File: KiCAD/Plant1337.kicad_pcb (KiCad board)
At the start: 4 copper layers, 59.1 x 41.9 mm, 58 parts, among them J1 USB_B_Micro, J2 Edge2x6_Connector, Q1 AO3400A, Q2 AO3400A, Q3 AO3400A, Q4 AO3400A, U1 SHTC3, U2 ESP32-WROOM-32, U3 AMS1117-3.3

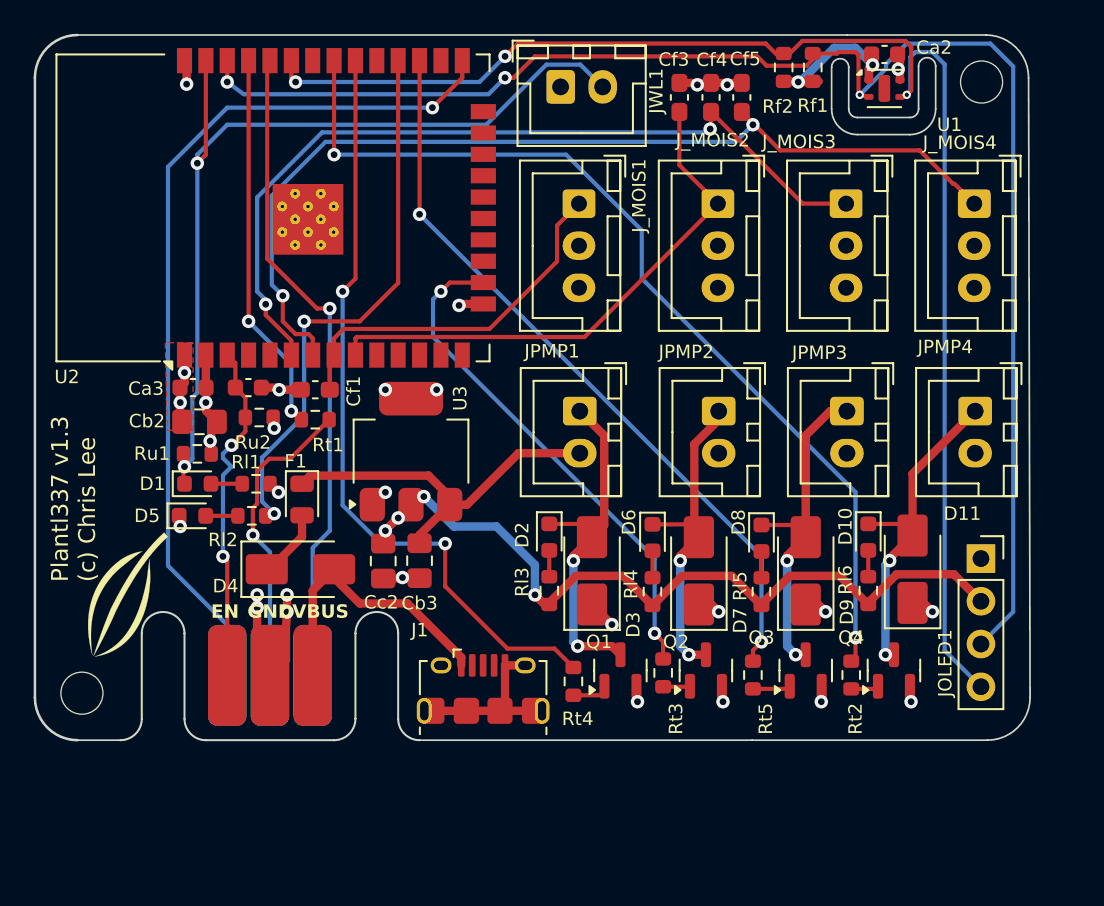
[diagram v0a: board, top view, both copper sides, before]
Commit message: Support for board 2.0: USB-C, ESP32-C3-WROOM1-B8R2
Need to make new board version a new compiler def and ifdef new pin assignments.
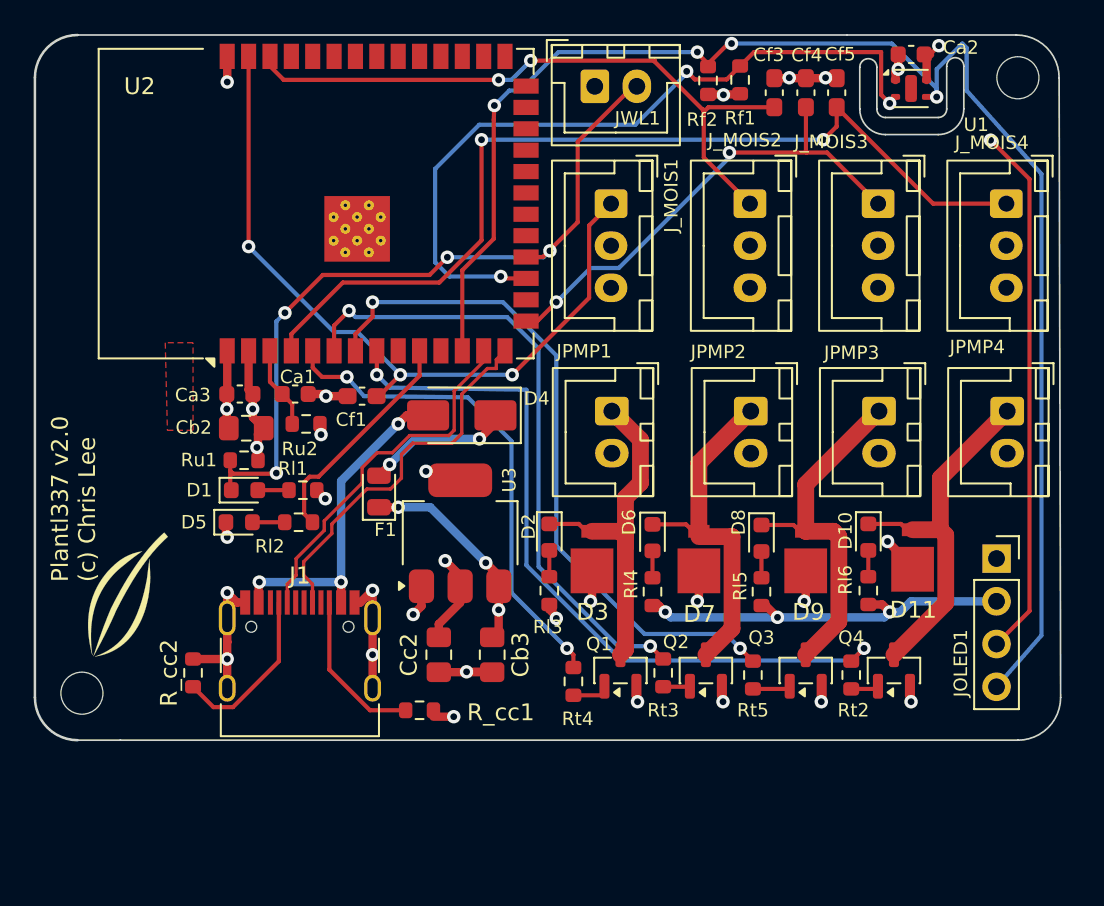
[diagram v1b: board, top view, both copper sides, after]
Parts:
- removed J2: Edge2x6_Connector, Library:EdgeConnector_2x3
- removed Rt1: 470, Resistor_SMD:R_0603_1608Metric
- added R_cc1: 5.1k, Resistor_SMD:R_0603_1608Metric, F.Cu at (69.8, 99.8)
- added R_cc2: 5.1k, Resistor_SMD:R_0603_1608Metric, F.Cu at (56.4, 97.6)
- D11, D3, D7, D9: footprint Diode_SMD:D_SMA -> chl33_library:DO-216
- J1: value USB_B_Micro -> USB_C_Receptacle_USB2.0_16P; footprint Connector_USB:USB_Micro-B_Amphenol_10118194_Horizontal -> Connector_USB:USB_C_Receptacle_HRO_TYPE-C-31-M-12
- U2: value ESP32-WROOM-32 -> ESP32-S3-WROOM-1; footprint RF_Module:ESP32-WROOM-32 -> RF_Module:ESP32-S3-WROOM-1
- moved D4 13.2 mm to (72.4, 82.3), turned to 180 degrees
- moved J1 10.9 mm to (62.7, 97.5)
- moved Cb3 7.06 mm to (74.2, 96.5)
- moved Cc2 6.47 mm to (71.0, 96.5)
- moved U3 5.66 mm to (72.3, 89.3)
- moved Cf3 5.65 mm to (90.9, 63.1)
- moved Cf4 5.65 mm to (92.8, 63.1)
- moved Cf5 5.65 mm to (94.6, 63.1)
- moved F1 4.60 mm to (67.4, 86.8), turned to 90 degrees
- moved Rf2 4.56 mm to (87.0, 62.4)
- moved Rf1 4.38 mm to (88.9, 62.4)
- moved D1 2.81 mm to (59.4, 86.7)
- moved Ca1 2.81 mm to (62.5, 81.0)
- moved Ca3 2.81 mm to (59.2, 81.0)
- moved Cb2 2.81 mm to (59.5, 83.1)
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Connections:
- U2 pad 10: unconnected-(U2-IO25-Pad10) -> GPIO17
- U2 pad 12: unconnected-(U2-IO27-Pad12) -> SDA1
- U2 pad 13: unconnected-(U2-IO14-Pad13) -> USB_D-
- U2 pad 14: unconnected-(U2-IO12-Pad14) -> USB_D+
- U2 pad 15: GND -> ADC1_CH6
- U2 pad 16: P2 -> unconnected-(U2-IO46-Pad16)
- U2 pad 17: unconnected-(U2-SHD/SD2-Pad17) -> SCL1
- U2 pad 18: unconnected-(U2-SWP/SD3-Pad18) -> WL
- U2 pad 25: GPIO0 -> unconnected-(U2-IO48-Pad25)
- U2 pad 27: P3 -> unconnected-(U2-IO0-Pad27)
- U2 pad 28: GPIO17 -> unconnected-(U2-IO35-Pad28)
- U2 pad 30: P1 -> unconnected-(U2-IO37-Pad30)
- U2 pad 31: P4 -> unconnected-(U2-IO38-Pad31)
- U2 pad 33: SDA1 -> unconnected-(U2-IO40-Pad33)
- U2 pad 34: TXC -> unconnected-(U2-IO41-Pad34)
- U2 pad 35: TX -> unconnected-(U2-IO42-Pad35)
- U2 pad 36: SCL1 -> unconnected-(U2-RXD0-Pad36)
- U2 pad 37: WL -> unconnected-(U2-TXD0-Pad37)
- U2 pad 38: GND -> ADC1_CH5
- U2 pad 39: GND -> ADC1_CH4
- U2 pad 4: unconnected-(U2-SENSOR_VP-Pad4) -> ADC1_CH7
- U2 pad 5: unconnected-(U2-SENSOR_VN-Pad5) -> P1
- U2 pad 6: ADC1_CH6 -> P2
- U2 pad 7: ADC1_CH7 -> P3
- U2 pad 8: ADC1_CH4 -> P4
- U2 pad 9: ADC1_CH5 -> unconnected-(U2-IO16-Pad9)
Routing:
- net GPIO0: track 52.4 -> 0.00 mm, vias 1 -> 0
- net TXC: track 39.0 -> 0.00 mm, vias 1 -> 0
- net TX: track 22.7 -> 0.00 mm, vias 2 -> 0
- net USB_D+: track 0.00 -> 22.6 mm
- net ADC1_CH4: track 22.3 -> 44.7 mm, vias 0 -> 3
- net USB_D-: track 0.00 -> 21.7 mm
- net ADC1_CH6: track 50.1 -> 29.2 mm
- net GPIO17: track 33.1 -> 13.5 mm, vias 2 -> 0
- net RXC: track 18.2 -> 0.00 mm, vias 1 -> 0
- net P1: track 45.9 -> 29.6 mm
- net EN: track 20.6 -> 4.89 mm, vias 2 -> 0
- net P4: track 56.7 -> 44.8 mm
- net Net-(J1-CC1): track 0.00 -> 10.2 mm
- net Net-(J1-CC2): track 0.00 -> 9.53 mm
- net +3.3V: track 84.5 -> 93.6 mm
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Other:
- board size 59.1 x 41.9 mm -> 61 x 41.9 mm
- board text added: "Plantl337 v2.0 (c) Chris Lee"
- board text removed: "EN"
- board text removed: "GND"
- board text removed: "IO0"
- board text removed: "Plantl337 v1.3 (c) Chris Lee"
- board text removed: "RX"
- board text removed: "TX"
- board text removed: "VBUS"

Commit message: fixed size of PCB
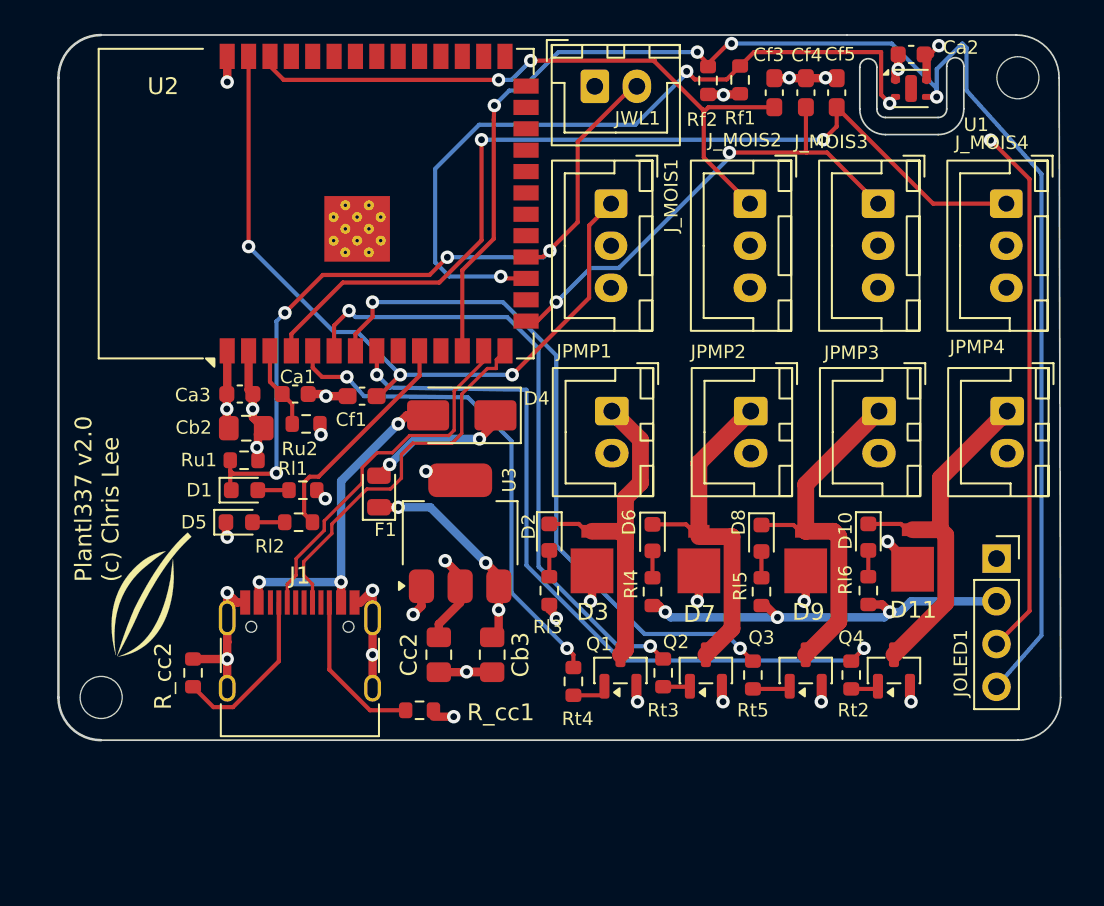
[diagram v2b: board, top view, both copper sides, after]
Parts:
- moved REF** 1.17 mm to (50.9, 99.1)
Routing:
- removed copper zone on F.Cu, net GND
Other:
- board size 61 x 41.9 mm -> 59.6 x 41.9 mm

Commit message: PCB v2.1: add push-buttons for prog/reset
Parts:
- added Ru4: 10k, Resistor_SMD:R_0603_1608Metric, F.Cu at (72.7, 100.5)
- added SW_EN1: SW_Push, Button_Switch_SMD:SW_SPST_FSMSM, F.Cu at (62.1, 97.5)
- added SW_PRG1: SW_Push, Button_Switch_SMD:SW_SPST_FSMSM, F.Cu at (80.0, 104.5)
- moved J1 8.01 mm to (62.7, 105.5)
- moved REF** 5.08 mm to (50.9, 104.1)
- moved R_cc2 4.37 mm to (56.4, 102.0)
- moved R_cc1 4.32 mm to (69.8, 104.1)
- moved U3 0.63 mm to (72.9, 89.3)
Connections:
- net EN renamed Net-(U2-EN)
- J1 pad A6: unconnected-(J1-D+-PadA6) -> USB_D+
- J1 pad A7: unconnected-(J1-D--PadA7) -> USB_D-
- U2 pad 27: unconnected-(U2-IO0-Pad27) -> Net-(U2-IO0)
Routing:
- net Net-(U2-IO0): track 0.00 -> 62.7 mm, vias 0 -> 2
- net Net-(U2-EN): track 4.89 -> 21.7 mm, vias 0 -> 2
- net USB_D-: track 21.7 -> 33.0 mm
- net USB_D+: track 22.6 -> 32.0 mm
- net VBUS: track 20.5 -> 28.5 mm
- net +3.3V: track 93.6 -> 98.2 mm, vias 12 -> 14
- net Net-(J1-CC2): track 9.53 -> 6.42 mm
- net Net-(J1-CC1): track 10.2 -> 7.27 mm
- net +5V: track 20.4 -> 21.2 mm, vias 7 -> 6
- net GND: track 52.7 -> 52.5 mm, vias 18 -> 20
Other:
- board size 59.6 x 41.9 mm -> 59.6 x 48.3 mm
- board text added: "Plantl337 v2.1 (c) Chris Lee"
- board text removed: "Plantl337 v2.0 (c) Chris Lee"
